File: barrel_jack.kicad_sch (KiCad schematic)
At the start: 16 parts, among them J10 Barrel_Jack, U1 MPQ9841GLE-5-AEC1-Z

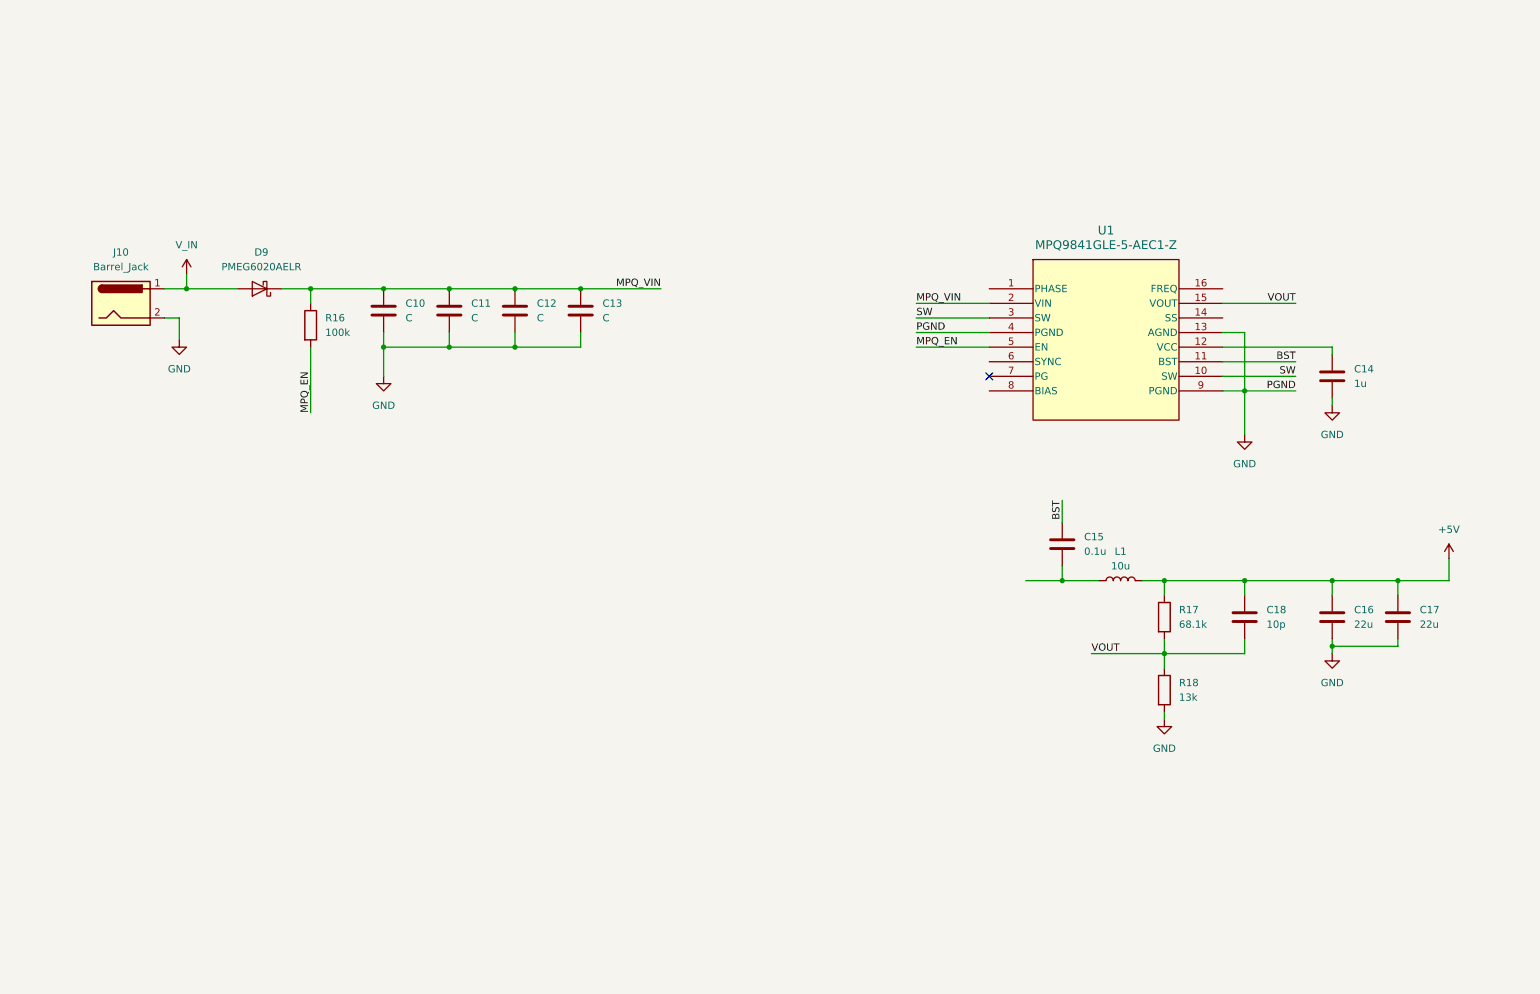
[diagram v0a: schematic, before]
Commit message: NCP1117-3.3 change
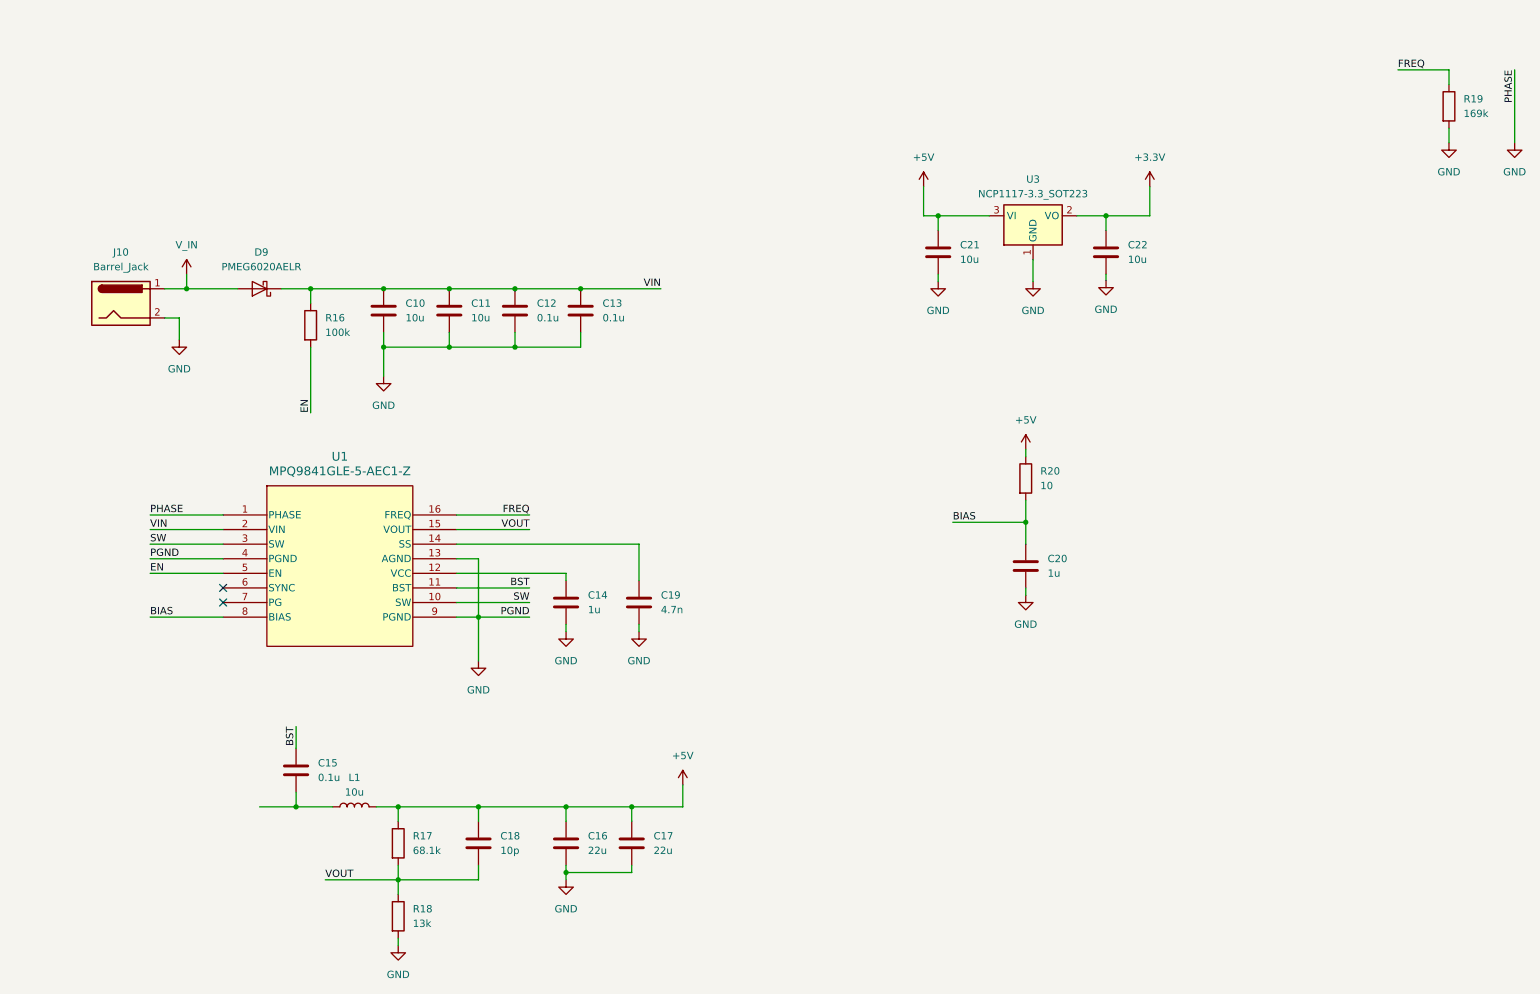
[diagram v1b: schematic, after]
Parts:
- added C19: 4.7n, symbol Device:C
- added C20: 1u, symbol Device:C
- added C21, C22: 10u, symbol Device:C
- added R19: 169k, symbol Device:R
- added R20: 10, symbol Device:R
- added U3: NCP1117-3.3_SOT223, Package_TO_SOT_SMD:SOT-223-3_TabPin2, symbol Regulator_Linear:NCP1117-3.3_SOT223
- C10, C11: value C -> 10u
- C12, C13: value C -> 0.1u
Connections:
- net +5V: now also C21.1, R20.1, U3.3 (VI)
- net GND: now also U1.1 (PHASE), C19.2, C20.2, C21.2, C22.2, R19.2, U3.1 (GND)
- net at U1.14 (SS): now also C19.1
- net FREQ: now reaches U1.16 (FREQ)
- net FREQ: now also R19.1
- net BIAS: now reaches U1.8 (BIAS)
- net BIAS: now also C20.1, R20.2
- net MPQ_EN renamed EN
- net MPQ_VIN renamed VIN
- new net +3.3V: C22.1, U3.2 (VO)
- no-connect marks 1 -> 2
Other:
- moved on the sheet: C14, C15, C16, C17, C18, L1, R17, R18, U1

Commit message: header pins + footprint assignment
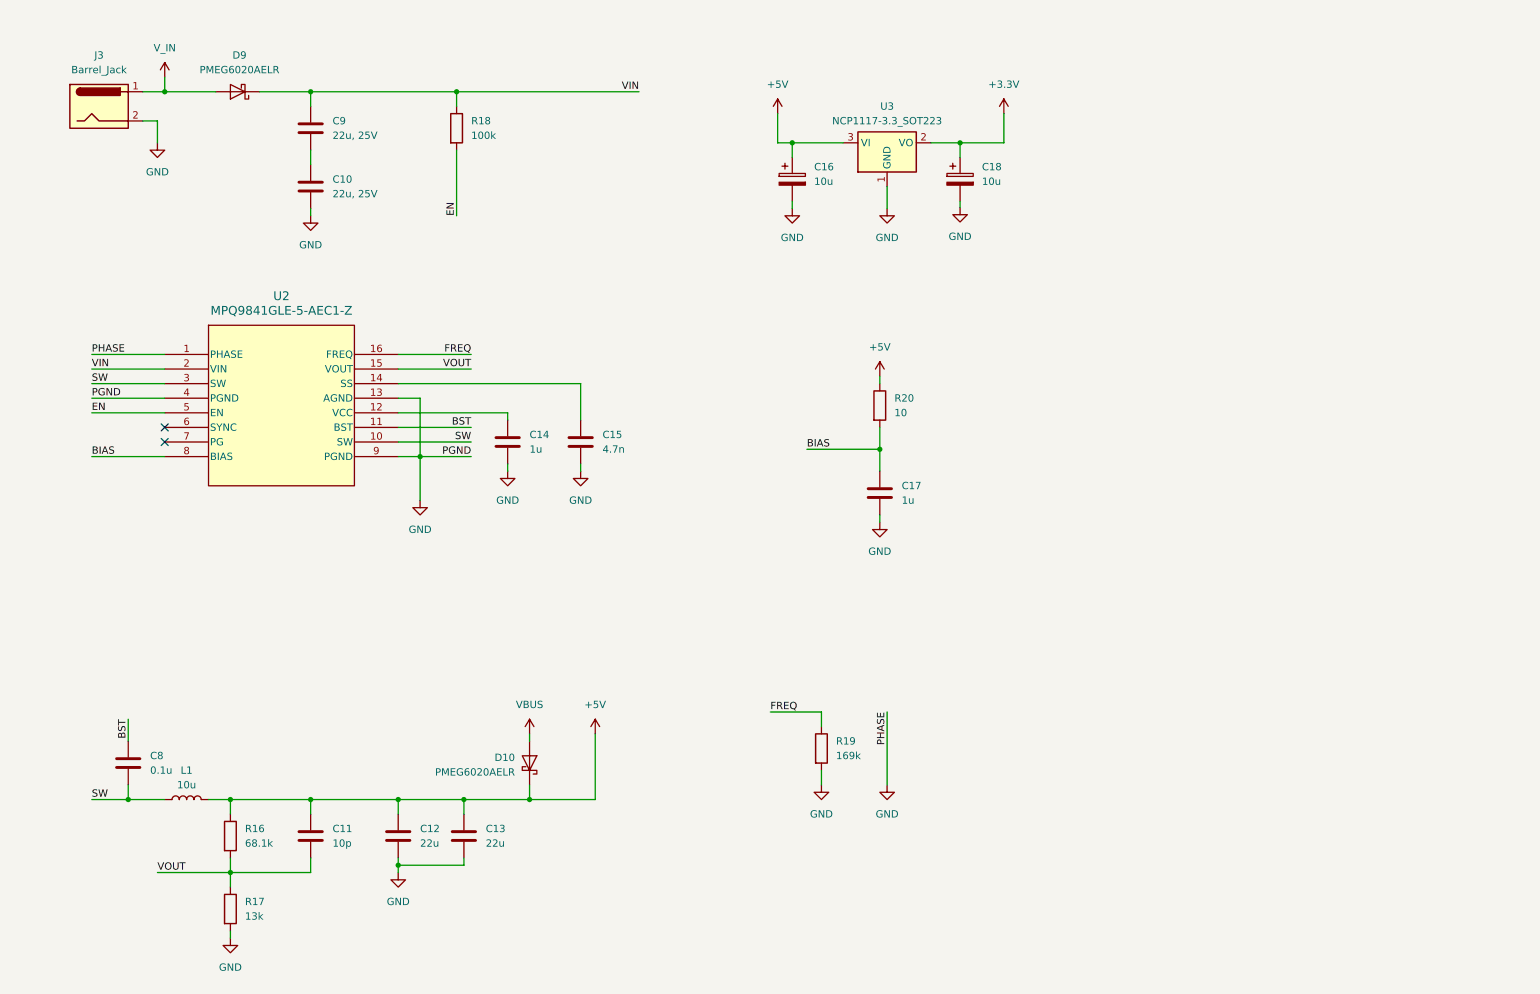
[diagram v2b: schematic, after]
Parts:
- removed C11: 10u, symbol Device:C
- removed C12, C13: 0.1u, symbol Device:C
- added C9: 22u, 25V, Capacitor_SMD:C_Elec_4x5.4, symbol Device:C
- added D10: PMEG6020AELR, Diode_SMD:Nexperia_CFP3_SOD-123W, symbol Diode:PMEG6020AELR
- C10: value 10u -> 22u, 25V; footprint (none) -> Capacitor_SMD:C_Elec_4x5.4
- C11: renamed from C18; footprint (none) -> Capacitor_SMD:C_0402_1005Metric
- C12: renamed from C16; footprint (none) -> Capacitor_SMD:C_Elec_5x5.8
- C13: renamed from C17; footprint (none) -> Capacitor_SMD:C_Elec_5x5.8
- C14: footprint (none) -> Capacitor_SMD:C_0603_1608Metric
- C15: renamed from C19; footprint (none) -> Capacitor_SMD:C_0402_1005Metric
- C16: renamed from C21; footprint (none) -> Capacitor_Tantalum_SMD:CP_EIA-3528-12_Kemet-T; symbol Device:C -> Device:C_Polarized
- C17: renamed from C20; footprint (none) -> Capacitor_SMD:C_0402_1005Metric
- C18: renamed from C22; footprint (none) -> Capacitor_Tantalum_SMD:CP_EIA-3528-12_Kemet-T; symbol Device:C -> Device:C_Polarized
- C8: renamed from C15; footprint (none) -> Capacitor_SMD:C_0603_1608Metric
- J3: renamed from J10; footprint (none) -> uno-esp:TENSILITY_54-00166
- L1: footprint (none) -> Inductor_SMD:L_Coilcraft_MSS1278T-XXX
- R16: renamed from R17; footprint (none) -> Resistor_SMD:R_0603_1608Metric
- R17: renamed from R18; footprint (none) -> Resistor_SMD:R_0402_1005Metric
- R18: renamed from R16; footprint (none) -> Resistor_SMD:R_0603_1608Metric
- R19: footprint (none) -> Resistor_SMD:R_0805_2012Metric
- R20: footprint (none) -> Resistor_SMD:R_0201_0603Metric
- U2: renamed from U1; footprint QFN-16_MPQ9841 -> uno-esp:QFN-16_MPQ9841
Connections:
- net +5V: now also D10.1 (K)
- net VIN: now also C9.1; no longer C10.1
- net at U2.10 (SW), U2.3 (SW): now also C8.2, L1.1
- new net: C10.1, C9.2
- new net VBUS: D10.2 (A)
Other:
- moved on the sheet: C11, C12, C13, C14, C15, C17, C8, D9, J3, L1, R16, R17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

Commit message: pcb component layout
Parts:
- removed J3: Barrel_Jack, uno-esp:TENSILITY_54-00166, symbol Connector:Barrel_Jack
- added D15: LED, LED_SMD:LED_0201_0603Metric, symbol Device:LED
- added J3: 54-00166, uno-esp:TENSILITY_54-00166, symbol 54-00166:54-00166
- added R23: 5.1k, Resistor_SMD:R_0201_0603Metric, symbol Device:R
- L1: footprint Inductor_SMD:L_Coilcraft_MSS1278T-XXX -> Inductor_SMD:L_Changjiang_FNR6045S
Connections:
- net +3.3V: now also R23.1
- net GND: now also D15.1 (K), J3.B, J3.C
- net V_IN: now also J3.A
- new net: D15.2 (A), R23.2

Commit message: layout + power pin traces
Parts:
- C11, C15, C17: footprint Capacitor_SMD:C_0402_1005Metric -> Capacitor_SMD:C_0201_0603Metric
- C12, C13: footprint Capacitor_SMD:C_Elec_5x5.8 -> Capacitor_SMD:C_0805_2012Metric
- C14: footprint Capacitor_SMD:C_0603_1608Metric -> Capacitor_SMD:C_0201_0603Metric
- R16: footprint Resistor_SMD:R_0603_1608Metric -> Resistor_SMD:R_0201_0603Metric
- R17: footprint Resistor_SMD:R_0402_1005Metric -> Resistor_SMD:R_0201_0603Metric
- R19: footprint Resistor_SMD:R_0805_2012Metric -> Resistor_SMD:R_0201_0603Metric
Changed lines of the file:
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@@
 			)
 		)
-		(property "Footprint" "Capacitor_SMD:C_0402_1005Metric"
+		(property "Footprint" "Capacitor_SMD:C_0201_0603Metric"
 			(at 67.0052 162.56 0)
 			(effects
@@
 			)
 		)
-		(property "Datasheet" "~"
+		(property "Datasheet" ""
 			(at 66.04 158.75 0)
 			(effects
@@
 			)
 		)
-		(property "Description" "Unpolarized capacitor"
+		(property "Description" ""
 			(at 66.04 158.75 0)
 			(effects
@@
 			)
 		)
-		(property "Footprint" "Capacitor_SMD:C_0402_1005Metric"
+		(property "Footprint" "Capacitor_SMD:C_0201_0603Metric"
 			(at 113.9952 93.98 0)
 			(effects
@@
 			)
 		)
-		(property "Datasheet" "~"
+		(property "Datasheet" ""
 			(at 113.03 90.17 0)
 			(effects
@@
 			)
 		)
-		(property "Description" "Unpolarized capacitor"
+		(property "Description" ""
 			(at 113.03 90.17 0)
 			(effects
@@
 			)
 		)
-		(property "Footprint" "Capacitor_SMD:C_0603_1608Metric"
+		(property "Footprint" "Capacitor_SMD:C_0201_0603Metric"
 			(at 101.2952 93.98 0)
 			(effects
@@
 			)
 		)
-		(property "Datasheet" "~"
+		(property "Datasheet" ""
 			(at 100.33 90.17 0)
 			(effects
@@
 			)
 		)
-		(property "Description" "Unpolarized capacitor"
+		(property "Description" ""
 			(at 100.33 90.17 0)
 			(effects
@@
 			)
 		)
-		(property "Footprint" "Capacitor_SMD:C_Elec_5x5.8"
+		(property "Footprint" "Capacitor_SMD:C_0805_2012Metric"
 			(at 93.6752 162.56 0)
 			(effects
@@
 			)
 		)
-		(property "Datasheet" "~"
+		(property "Datasheet" ""
 			(at 92.71 158.75 0)
 			(effects
@@
 			)
 		)
-		(property "Description" "Unpolarized capacitor"
+		(property "Description" ""
 			(at 92.71 158.75 0)
 			(effects
@@
 			)
 		)
-		(property "Footprint" "Resistor_SMD:R_0603_1608Metric"
+		(property "Footprint" "Resistor_SMD:R_0201_0603Metric"
 			(at 50.292 158.75 90)
 			(effects
@@
 			)
 		)
-		(property "Datasheet" "~"
+		(property "Datasheet" ""
 			(at 52.07 158.75 0)
 			(effects
@@
 			)
 		)
-		(property "Description" "Resistor"
+		(property "Description" ""
 			(at 52.07 158.75 0)
 			(effects
@@
 			)
 		)
-		(property "Footprint" "Capacitor_SMD:C_Elec_5x5.8"
+		(property "Footprint" "Capacitor_SMD:C_0805_2012Metric"
 			(at 82.2452 162.56 0)
 			(effects
@@
 			)
 		)
-		(property "Datasheet" "~"
+		(property "Datasheet" ""
 			(at 81.28 158.75 0)
 			(effects
@@
 			)
 		)
-		(property "Description" "Unpolarized capacitor"
+		(property "Description" ""
 			(at 81.28 158.75 0)
 			(effects
@@
 			)
 		)
-		(property "Footprint" "Capacitor_SMD:C_0402_1005Metric"
+		(property "Footprint" "Capacitor_SMD:C_0201_0603Metric"
 			(at 166.0652 102.87 0)
 			(effects
@@
 			)
 		)
-		(property "Datasheet" "~"
+		(property "Datasheet" ""
 			(at 165.1 99.06 0)
 			(effects
@@
 			)
 		)
-		(property "Description" "Unpolarized capacitor"
+		(property "Description" ""
 			(at 165.1 99.06 0)
 			(effects
@@
 			)
 		)
-		(property "Footprint" "Resistor_SMD:R_0805_2012Metric"
+		(property "Footprint" "Resistor_SMD:R_0201_0603Metric"
 			(at 153.162 143.51 90)
 			(effects
@@
 			)
 		)
-		(property "Datasheet" "~"
+		(property "Datasheet" ""
 			(at 154.94 143.51 0)
 			(effects
@@
 			)
 		)
-		(property "Description" "Resistor"
+		(property "Description" ""
 			(at 154.94 143.51 0)
 			(effects
@@
 			)
 		)
-		(property "Footprint" "Resistor_SMD:R_0402_1005Metric"
+		(property "Footprint" "Resistor_SMD:R_0201_0603Metric"
 			(at 50.292 171.45 90)
 			(effects
@@
 			)
 		)
-		(property "Datasheet" "~"
+		(property "Datasheet" ""
 			(at 52.07 171.45 0)
 			(effects
@@
 			)
 		)
-		(property "Description" "Resistor"
+		(property "Description" ""
 			(at 52.07 171.45 0)
 			(effects

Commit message: final tracing + pcb layers + colors
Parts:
- removed D10: PMEG6020AELR, Diode_SMD:Nexperia_CFP3_SOD-123W, symbol Diode:PMEG6020AELR
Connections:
- net V_IN is gone; now on net VIN: D9.2 (A), J3.A
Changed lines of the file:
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@@
-	)
-	(junction
-		(at 104.14 152.4)
-		(diameter 0)
-		(color 0 0 0 0)
 	)
 	(junction
@@
 	(wire
 		(pts
-			(xy 104.14 140.97) (xy 104.14 142.24)
-		)
-		(stroke
-			(width 0)
-			(type default)
-		)
-	)
-	(wire
-		(pts
 			(xy 66.04 152.4) (xy 66.04 154.94)
 		)
@@
 	(wire
 		(pts
-			(xy 104.14 149.86) (xy 104.14 152.4)
-		)
-		(stroke
-			(width 0)
-			(type default)
-		)
-	)
-	(wire
-		(pts
-			(xy 92.71 152.4) (xy 104.14 152.4)
+			(xy 92.71 152.4) (xy 115.57 152.4)
 		)
 		(stroke
@@
 		(pts
 			(xy 39.37 165.1) (xy 52.07 165.1)
-		)
-		(stroke
-			(width 0)
-			(type default)
-		)
-	)
-	(wire
-		(pts
-			(xy 104.14 152.4) (xy 115.57 152.4)
 		)
 		(stroke
@@
 			)
 		)
-		(property "Value" "V_IN"
+		(property "Value" "VIN"
 			(at 44.45 21.59 0)
 			(effects
@@
 	)
 	(symbol
-		(lib_id "Diode:PMEG6020AELR")
-		(at 104.14 146.05 270)
-		(mirror x)
-		(unit 1)
-		(exclude_from_sim no)
-		(in_bom yes)
-		(on_board yes)
-		(dnp no)
-		(property "Reference" "D10"
-			(at 101.6 145.0974 90)
-			(effects
-				(font
-					(size 1.27 1.27)
-				)
-				(justify right)
-			)
-		)
-		(property "Value" "PMEG6020AELR"
-			(at 101.6 147.6374 90)
-			(effects
-				(font
-					(size 1.27 1.27)
-				)
-				(justify right)
-			)
-		)
-		(property "Footprint" "Diode_SMD:Nexperia_CFP3_SOD-123W"
-			(at 99.695 146.05 0)
-			(effects
-				(font
-					(size 1.27 1.27)
-				)
-				(hide yes)
-			)
-		)
-		(property "Datasheet" "https://assets.nexperia.com/documents/data-sheet/PMEG6020AELR.pdf"
-			(at 104.14 146.05 0)
-			(effects
-				(font
-					(size 1.27 1.27)
-				)
-				(hide yes)
-			)
-		)
-		(property "Description" "60V, 2A low leakage current MEGA Schottky barrier rectifier, SOD-123W"
-			(at 104.14 146.05 0)
-			(effects
-				(font
-					(size 1.27 1.27)
-				)
-				(hide yes)
-			)
-		)
-		(pin "1"
-		)
-		(pin "2"
-		)
-		(instances
-			(project "esp32-c6"
-				(path "/98d6a3bc-4267-493f-8210-1fe038eb9de4/9ae47cac-932a-49fb-9366-e71a08cd92a9"
-					(reference "D10")
-					(unit 1)
-				)
-			)
-		)
-	)
-	(symbol
 		(lib_id "Device:C")
 		(at 100.33 90.17 0)
@@
 					(unit 1)
 				)
-			)
-		)
-	)
-	(symbol
-		(lib_id "power:VBUS")
-		(at 104.14 140.97 0)
-		(unit 1)
-		(exclude_from_sim no)
-		(in_bom yes)
-		(on_board yes)
-		(dnp no)
-		(fields_autoplaced yes)
-		(property "Reference" "#PWR038"
-			(at 104.14 144.78 0)
-			(effects
-				(font
-					(size 1.27 1.27)
-				)
-				(hide yes)
-			)
-		)
-		(property "Value" "VBUS"
-			(at 104.14 135.89 0)
-			(effects
-				(font
-					(size 1.27 1.27)
-				)
-			)
-		)
-		(property "Footprint" ""
-			(at 104.14 140.97 0)
-			(effects
-				(font
-					(size 1.27 1.27)
-				)
-				(hide yes)
-			)
-		)
-		(property "Datasheet" ""
-			(at 104.14 140.97 0)
-			(effects
-				(font
-					(size 1.27 1.27)
-				)
-				(hide yes)
-			)
-		)
-		(property "Description" "Power symbol creates a global label with name \"VBUS\""
-			(at 104.14 140.97 0)
-			(effects
-				(font
-					(size 1.27 1.27)
-				)
-				(hide yes)
-			)
-		)
-		(pin "1"
-		)
-		(instances
-			(project ""
-				(path "/98d6a3bc-4267-493f-8210-1fe038eb9de4/9ae47cac-932a-49fb-9366-e71a08cd92a9"
-					(reference "#PWR038")
-					(unit 1)
-				)

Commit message: Refinement to pcb and schematic layout
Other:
- title: (none) -> ESP32-C6 Dev Board
- moved on the sheet: C11, C12, C13, C14, C15, C16, C17, C18, C8, D15, L1, R16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
